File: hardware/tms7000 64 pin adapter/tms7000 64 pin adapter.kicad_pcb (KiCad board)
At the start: 2 copper layers, 40.5 x 52.1 mm, 4 parts, among them J1 plcc 68, U1 DIP40 male pins

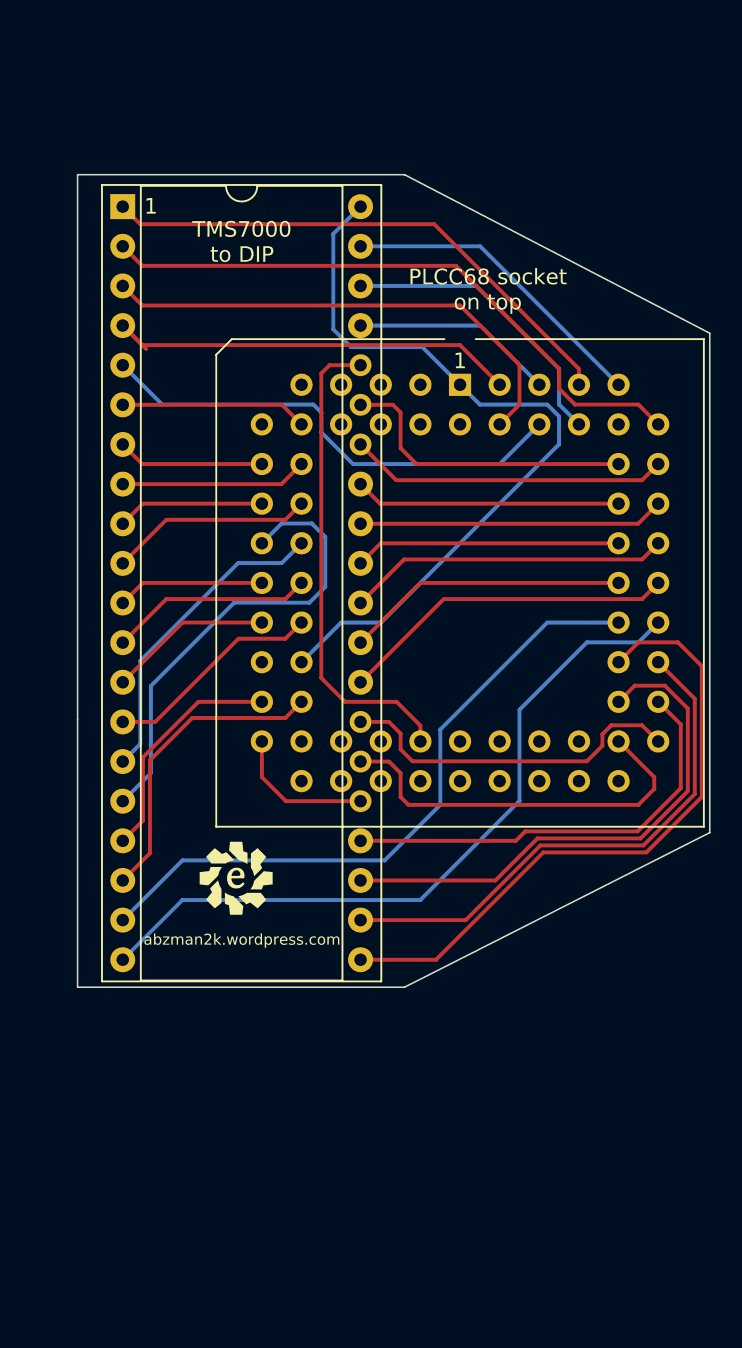
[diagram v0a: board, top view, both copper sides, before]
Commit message: fixed plcc88, added qfp60, dip54, dip64, and dip64 small pitch
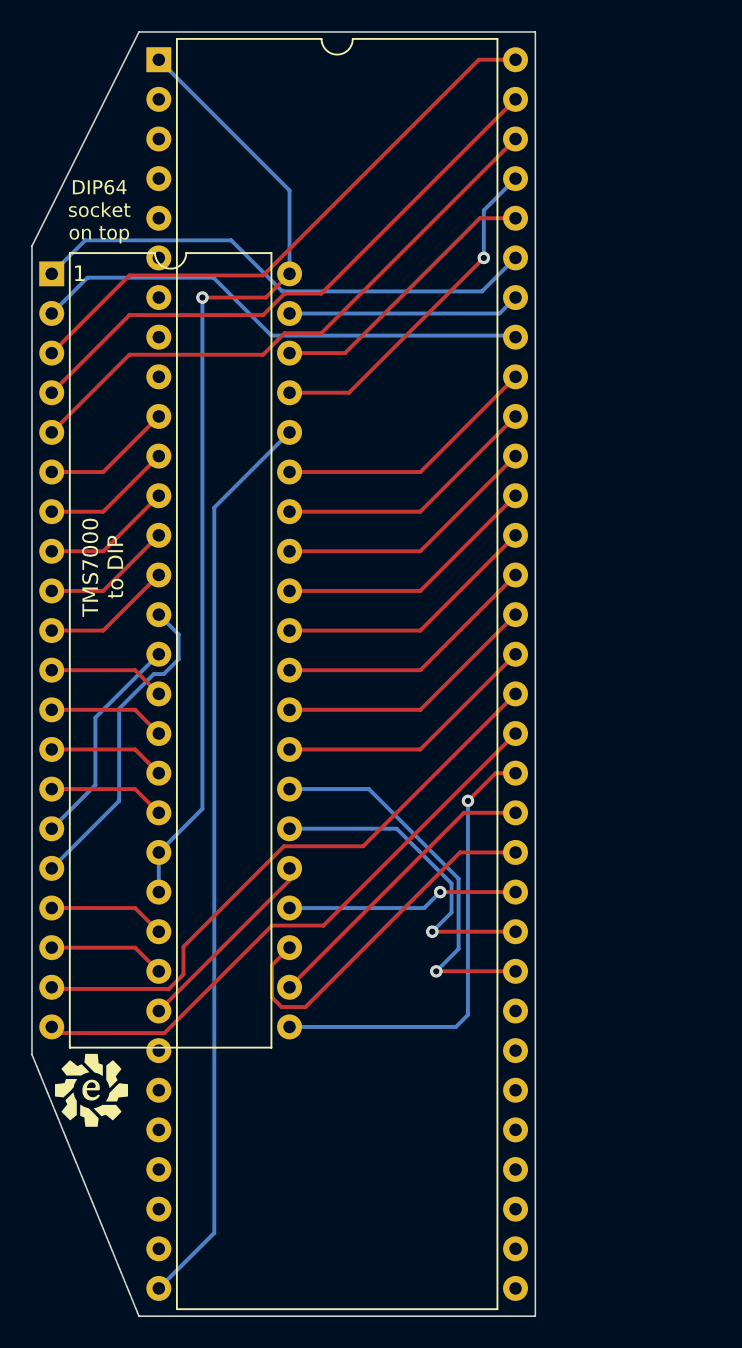
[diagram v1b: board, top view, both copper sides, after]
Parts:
- J1: value plcc 68 -> DIP64; footprint Package_LCC:PLCC-68_THT-Socket -> Package_DIP:DIP-64_W22.86mm
- U1: footprint Package_DIP:DIP-40_W15.24mm_Socket -> Package_DIP:DIP-40_W15.24mm
- moved J1 28.4 mm to (122.4, 39.1)
- moved G*** 16.6 mm to (118.4, 104.9)
- moved G*** 16.5 mm to (118.1, 105.2)
- moved U1 6.26 mm to (115.6, 52.8)
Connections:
- J1 pad 10: F7 -> A0
- J1 pad 11: A0 -> A1
- J1 pad 12: A1 -> A2
- J1 pad 13: A2 -> A3
- J1 pad 14: A3 -> A4
- J1 pad 15: A4 -> A5
- J1 pad 16: A5 -> A6
- J1 pad 17: A6 -> A7
- J1 pad 18: A7 -> /INT3
- J1 pad 19: /INT3 -> /INT1
- J1 pad 20: /INT1 -> /RESET
- J1 pad 21: /RESET -> Vss
- J1 pad 22: /HALT -> Vss
- J1 pad 23: Vss -> XTAL2
- J1 pad 24: XTAL2 -> XTAL1
- J1 pad 25: XTAL1 -> Vcc
- J1 pad 26: Vcc -> G0
- J1 pad 27: G0 -> G1
- J1 pad 28: unconnected-(J1-Pad28) -> G2
- J1 pad 29: G1 -> G3
- J1 pad 30: G2 -> G4
- J1 pad 31: G3 -> G5
- J1 pad 32: G4 -> MC
- J1 pad 33: G5 -> E0
- J1 pad 34: MC -> E1
- J1 pad 35: E0 -> E2
- J1 pad 36: E1 -> E3
- J1 pad 37: E2 -> E4
- J1 pad 38: E3 -> E5
- J1 pad 39: E4 -> E6
- J1 pad 40: E5 -> E7
- J1 pad 41: E6 -> D0
- J1 pad 42: E7 -> D1
- J1 pad 43: unconnected-(J1-Pad43) -> D2
- J1 pad 44: D0 -> D3
- J1 pad 45: D1 -> D4
- J1 pad 46: D2 -> D5
- J1 pad 47: D3 -> D6
- J1 pad 48: D4 -> D7
- J1 pad 49: D5 -> C0
- J1 pad 50: D6 -> C1
- J1 pad 51: D7 -> C2
- J1 pad 52: C0 -> C3
- J1 pad 53: C1 -> C4
- J1 pad 54: C2 -> C5
- J1 pad 55: C3 -> C6
- J1 pad 56: C4 -> C7
- J1 pad 57: C5 -> B7
- J1 pad 58: C6 -> B6
- J1 pad 59: C7 -> B5
- J1 pad 60: B7 -> B4
- J1 pad 61: B6 -> B3
- J1 pad 62: unconnected-(J1-Pad62) -> B2
- J1 pad 63: B5 -> B1
- J1 pad 64: B4 -> B0
- J1 pad 9: unconnected-(J1-Pad9) -> F7
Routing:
- net MC: track 30.9 -> 58.3 mm
- net D4: track 34.2 -> 19.1 mm
- net Vss: track 49.4 -> 62.7 mm, vias 0 -> 1
- net D2: track 28.1 -> 14.9 mm, vias 0 -> 1
- net XTAL1: track 19.7 -> 7.49 mm
- net D5: track 41.1 -> 29.3 mm, vias 0 -> 1
- net D3: track 34.1 -> 23.6 mm
- net B1: track 27.9 -> 37.5 mm
- net A5: track 30.1 -> 20.5 mm
- net B3: track 13.0 -> 22.0 mm, vias 0 -> 1
- net D6: track 46.7 -> 37.8 mm
- net B7: track 39.8 -> 32.3 mm
- net XTAL2: track 15.0 -> 7.49 mm
- net /RESET: track 14.1 -> 7.49 mm
- net B2: track 31.1 -> 37.5 mm
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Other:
- board size 40.5 x 52.1 mm -> 32.3 x 82.3 mm
- board text added: "DIP64 socket on top"
- board text removed: "PLCC68 socket on top"
